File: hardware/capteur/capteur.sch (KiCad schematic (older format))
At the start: 38 parts, among them J1 Pluvio, J10 RJ45, J11 Term_sel, J12 Conn_01x05_Male, J2 Conn_01x02_Male, J3 NMEA0183 (wind), J4 Conn_01x02_Male, J5 Conn_01x02_Male, J6 Conn_01x02_Male, J7 Conn_01x03_Male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

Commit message: L'empreinte utilisée pour le connecteur RJ45 MP002453 est inversée; modification du nom utilisé pour le montrer.
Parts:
- J10: footprint local:multicomp_MP002453 -> local:multicomp_MP002453-swappedpins
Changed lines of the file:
@@
 F 0 "J10" H 9270 4046 50  0000 R CNN
 F 1 "RJ45" H 9270 3955 50  0000 R CNN
-F 2 "local:multicomp_MP002453" V 9600 3975 50  0001 C CNN
+F 2 "local:multicomp_MP002453-swappedpins" V 9600 3975 50  0001 C CNN
 F 3 "~" V 9600 3975 50  0001 C CNN
 	1    9600 3950

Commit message: Nome les signaux SCL et SDA (pour repérage facile)
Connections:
- net SCL: now reaches J9.2 (Pin_2), R6.2, U1.14 (SCL/SCK/RC3)
- net SDA: now reaches J9.1 (Pin_1), R5.2, U1.15 (SDA/SDI/RC4)
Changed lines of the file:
@@
 	5400 5150 5400 5250
 Connection ~ 5400 5150
+Text Label 5450 4950 0    50   ~ 0
+SCL
+Text Label 5450 5050 0    50   ~ 0
+SDA
 $EndSCHEMATC

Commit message: capteur: Update schematic for v2 switch to pic18f27q84, change CAN transeiver reference (it's pin-compatible), switch regulators to LDL1117S50/mic5504-3.3. Also use a RJ45 connector with the right pinout.
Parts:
- removed C5: 10uF, Capacitor_SMD:C_1210_3225Metric_Pad1.33x2.70mm_HandSolder, symbol Device:C_Small
- C10, C9: value 10uF -> 1uF; footprint Capacitor_SMD:C_1210_3225Metric_Pad1.33x2.70mm_HandSolder -> Capacitor_SMD:C_0805_2012Metric_Pad1.18x1.45mm_HandSolder
- J10: footprint local:multicomp_MP002453-swappedpins -> local:multicomp_MP002453
- U1: value PIC18F26K80_ISS -> PIC18F27Q84_ISS; symbol MCU_Microchip_PIC18:PIC18F26K80_ISS -> microchip-local:PIC18F27Q84; P/N (none) -> PIC18F27Q84_ISS
- U2: value MCP2542FDxMF -> TLE9250VSJXUMA1; P/N (none) -> TLE9250VSJXUMA1
- U3: value uA7833 -> mic5504-3.3; footprint Package_TO_SOT_SMD:SOT-223-3_TabPin2 -> Package_TO_SOT_SMD:SOT-23-5_HandSoldering; symbol Regulator_Linear:uA7805 -> Regulator_Linear:MIC5504-3.3YM5; P/N (none) -> mic5504-3.3
- U4: value uA7805 -> LDL1117S50; symbol Regulator_Linear:uA7805 -> Regulator_Linear:LD1117S50TR_SOT223; P/N (none) -> LDL1117S50
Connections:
- net +12V: now also U4.3 (VI); no longer U3.1 (IN), U4.1 (IN)
- net +3V3: now also U3.5 (VOUT); no longer U3.3 (OUT)
- net +5V: now also U3.1 (VIN), U3.3 (EN), U4.2 (VO); no longer U4.3 (OUT)
- net GND: now also U4.1 (GND); no longer U4.2 (GND)
- net at C2.1, Y1.1: now also U1.9 (OSC1/CLKIN); no longer U1.10 (OSC2/CLKOUT)
- net at C3.1, Y1.2: now also U1.10 (OSC2/CLKOUT); no longer U1.9 (OSC1/CLKIN)
- no-connect marks 2 -> 3
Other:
- moved on the sheet: J2, R2
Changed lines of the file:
@@
 $EndDescr
-$Comp
-L MCU_Microchip_PIC18:PIC18F26K80_ISS U1
-U 1 1 604422A9
-P 4600 4550
-F 0 "U1" H 4600 5617 50  0000 C CNN
-F 1 "PIC18F26K80_ISS" H 4600 5526 50  0000 C CNN
-F 2 "Package_SO:SOIC-28W_7.5x17.9mm_P1.27mm" H 4600 4300 50  0001 C CNN
-F 3 "http://ww1.microchip.com/downloads/en/DeviceDoc/39977f.pdf" H 4600 4500 50  0001 C CNN
-	1    4600 4550
-	1    0    0    -1
-$EndComp
 $Comp
 L Interface_CAN_LIN:MCP2542FDxMF U2
@@
 P 6700 4150
 F 0 "U2" H 6850 3900 50  0000 C CNN
-F 1 "MCP2542FDxMF" H 7050 3750 50  0000 C CNN
+F 1 "TLE9250VSJXUMA1" H 7050 3750 50  0000 C CNN
 F 2 "Package_SO:SOIC-8_3.9x4.9mm_P1.27mm" H 6700 3650 50  0001 C CIN
-F 3 "http://ww1.microchip.com/downloads/en/DeviceDoc/MCP2542FD-4FD-MCP2542WFD-4WFD-Data-Sheet20005514B.pdf" H 6700 4150 50  0001 C CNN
+F 3 "" H 6700 4150 50  0001 C CNN
+F 4 "TLE9250VSJXUMA1" H 6700 4150 50  0001 C CNN "P/N"
 	1    6700 4150
 	1    0    0    -1
 $EndComp
 $Comp
-L Regulator_Linear:uA7805 U4
+L Regulator_Linear:LD1117S50TR_SOT223 U4
 U 1 1 604437C3
 P 8100 4000
 F 0 "U4" H 8100 4050 50  0000 C CNN
-F 1 "uA7805" H 8100 3600 50  0000 C CNN
+F 1 "LDL1117S50" H 8100 3750 50  0000 C CNN
 F 2 "Package_TO_SOT_SMD:SOT-223-3_TabPin2" H 8125 3850 50  0001 L CIN
-F 3 "http://www.ti.com/lit/ds/symlink/ua78.pdf" H 8100 3950 50  0001 C CNN
+F 3 "" H 8100 3950 50  0001 C CNN
+F 4 "LDL1117S50" H 8100 4000 50  0001 C CNN "P/N"
 	1    8100 4000
 	-1   0    0    1
@@
 	3150 4600 3150 4500
 $Comp
-L Device:C_Small C5
-U 1 1 60447786
-P 3550 5050
-F 0 "C5" H 3458 5004 50  0000 R CNN
-F 1 "10uF" H 3458 5095 50  0000 R CNN
-F 2 "Capacitor_SMD:C_1210_3225Metric_Pad1.33x2.70mm_HandSolder" H 3550 5050 50  0001 C CNN
-F 3 "~" H 3550 5050 50  0001 C CNN
-	1    3550 5050
-	-1   0    0    1
-$EndComp
-$Comp
 L Device:C_Small C4
 U 1 1 6044A0E3
@@
 Connection ~ 3700 4850
 Wire Wire Line
-	3800 4950 3550 4950
-Wire Wire Line
 	3850 5150 3800 5150
 Connection ~ 3800 5150
-Wire Wire Line
-	3800 5150 3550 5150
-Wire Wire Line
-	3550 5150 3400 5150
-Connection ~ 3550 5150
 Wire Wire Line
 	3400 5150 3150 5150
@@
 F 0 "J10" H 9270 4046 50  0000 R CNN
 F 1 "RJ45" H 9270 3955 50  0000 R CNN
-F 2 "local:multicomp_MP002453-swappedpins" V 9600 3975 50  0001 C CNN
+F 2 "local:multicomp_MP002453" V 9600 3975 50  0001 C CNN
 F 3 "~" V 9600 3975 50  0001 C CNN
 	1    9600 3950
@@
 P 7700 3850
 F 0 "C10" H 7850 3800 50  0000 R CNN
-F 1 "10uF" H 7950 3900 50  0000 R CNN
-F 2 "Capacitor_SMD:C_1210_3225Metric_Pad1.33x2.70mm_HandSolder" H 7700 3850 50  0001 C CNN
+F 1 "1uF" H 7950 3900 50  0000 R CNN
+F 2 "Capacitor_SMD:C_0805_2012Metric_Pad1.18x1.45mm_HandSolder" H 7700 3850 50  0001 C CNN
 F 3 "~" H 7700 3850 50  0001 C CNN
 	1    7700 3850
@@
 Connection ~ 8450 4000
 Connection ~ 8950 4050
-$Comp
-L Device:R_Small R2
-U 1 1 6048396A
-P 3500 4350
-F 0 "R2" V 3400 4350 50  0000 C CNN
-F 1 "10K" V 3500 4350 50  0000 C CNN
-F 2 "Resistor_THT:R_Axial_DIN0207_L6.3mm_D2.5mm_P7.62mm_Horizontal" H 3500 4350 50  0001 C CNN
-F 3 "~" H 3500 4350 50  0001 C CNN
-	1    3500 4350
-	0    1    1    0
-$EndComp
-$Comp
-L power:+3.3V #PWR03
-U 1 1 60484075
-P 3350 4300
-F 0 "#PWR03" H 3350 4150 50  0001 C CNN
-F 1 "+3.3V" H 3365 4473 50  0000 C CNN
-F 2 "" H 3350 4300 50  0001 C CNN
-F 3 "" H 3350 4300 50  0001 C CNN
-	1    3350 4300
-	1    0    0    -1
-$EndComp
-Wire Wire Line
-	3800 4350 3600 4350
-Wire Wire Line
-	3400 4350 3350 4350
-Wire Wire Line
-	3350 4350 3350 4300
-Text Label 3600 4350 0    50   ~ 0
-MCLR
 $Comp
 L Connector:Conn_01x05_Male J12
@@
 Wire Wire Line
 	8900 4000 8900 4050
-Wire Wire Line
-	8450 4000 8550 4000
-$Comp
-L Regulator_Linear:uA7805 U3
+$Comp
+L Regulator_Linear:MIC5504-3.3YM5 U3
 U 1 1 604B439A
 P 8100 3400
 F 0 "U3" H 8100 3450 50  0000 C CNN
-F 1 "uA7833" H 8100 3000 50  0000 C CNN
-F 2 "Package_TO_SOT_SMD:SOT-223-3_TabPin2" H 8125 3250 50  0001 L CIN
-F 3 "http://www.ti.com/lit/ds/symlink/ua78.pdf" H 8100 3350 50  0001 C CNN
+F 1 "mic5504-3.3" H 8100 3000 50  0000 C CNN
+F 2 "Package_TO_SOT_SMD:SOT-23-5_HandSoldering" H 8125 3250 50  0001 L CIN
+F 3 "" H 8100 3350 50  0001 C CNN
+F 4 "mic5504-3.3" H 8100 3400 50  0001 C CNN "P/N"
 	1    8100 3400
 	-1   0    0    1
@@
 P 7700 3250
 F 0 "C9" H 7850 3200 50  0000 R CNN
-F 1 "10uF" H 7950 3300 50  0000 R CNN
-F 2 "Capacitor_SMD:C_1210_3225Metric_Pad1.33x2.70mm_HandSolder" H 7700 3250 50  0001 C CNN
+F 1 "1uF" H 7950 3300 50  0000 R CNN
+F 2 "Capacitor_SMD:C_0805_2012Metric_Pad1.18x1.45mm_HandSolder" H 7700 3250 50  0001 C CNN
 F 3 "~" H 7700 3250 50  0001 C CNN
 	1    7700 3250
@@
 Wire Wire Line
 	7700 3400 7700 3350
-Connection ~ 7700 3400
-Wire Wire Line
-	7700 3400 7800 3400
 Wire Wire Line
 	7700 3150 7700 3100
@@
 Wire Wire Line
 	8650 3750 8450 3750
-Wire Wire Line
-	8550 3400 8550 4000
-Wire Wire Line
-	8400 3400 8550 3400
-Connection ~ 8550 4000
-Wire Wire Line
-	8550 4000 8900 4000
 $Comp
 L power:GND #PWR09
@@
 L Connector:Conn_01x02_Male J2
 U 1 1 605531D0
-P 3400 3750
-F 0 "J2" H 3508 3931 50  0000 C CNN
-F 1 "Conn_01x02_Male" H 3508 3840 50  0000 C CNN
-F 2 "te:282834-2_1" H 3400 3750 50  0001 C CNN
-F 3 "~" H 3400 3750 50  0001 C CNN
-	1    3400 3750
+P 3400 3850
+F 0 "J2" H 3350 3800 50  0000 C CNN
+F 1 "Conn_01x02_Male" H 3500 3700 50  0000 C CNN
+F 2 "te:282834-2_1" H 3400 3850 50  0001 C CNN
+F 3 "~" H 3400 3850 50  0001 C CNN
+	1    3400 3850
 	1    0    0    -1
 $EndComp
@@
 Connection ~ 3150 4500
 Wire Wire Line
-	3650 4000 3650 4150
-Wire Wire Line
-	3650 4150 3800 4150
-Wire Wire Line
-	3600 3750 3800 3750
-Wire Wire Line
-	3800 3850 3600 3850
+	3600 3850 3800 3850
+Wire Wire Line
+	3800 3950 3600 3950
 $Comp
 L Device:R_Small R1
@@
 	3050 4500 2850 4500
 Connection ~ 3050 4500
-Wire Wire Line
-	3650 4000 3050 4000
 Connection ~ 3050 4000
 Wire Wire Line
@@
 Wire Wire Line
 	3050 4000 2850 4000
-NoConn ~ 3800 3950
+NoConn ~ 3800 4250
 NoConn ~ 3800 4050
 $Comp
@@
 	1    0    0    -1
 $EndComp
-$Comp
-L power:PWR_FLAG #FLG01
-U 1 1 606683BC
-P 8550 3350
-F 0 "#FLG01" H 8550 3425 50  0001 C CNN
-F 1 "PWR_FLAG" H 8550 3523 50  0000 C CNN
-F 2 "" H 8550 3350 50  0001 C CNN
-F 3 "~" H 8550 3350 50  0001 C CNN
-	1    8550 3350
-	1    0    0    -1
-$EndComp
 Wire Wire Line
 	8650 3050 8650 3100
 Connection ~ 8650 3100
-Wire Wire Line
-	8550 3350 8550 3400
-Connection ~ 8550 3400
 $Comp
 L Connector_Generic:Conn_02x03_Odd_Even J11
@@
 	10700 4150 10850 4150
 $Comp
-L power:GND #PWR?
+L power:GND #PWR0101
 U 1 1 6069A878
 P 5500 5150
-F 0 "#PWR?" H 5500 4900 50  0001 C CNN
+F 0 "#PWR0101" H 5500 4900 50  0001 C CNN
 F 1 "GND" H 5505 4977 50  0000 C CNN
 F 2 "" H 5500 5150 50  0001 C CNN
@@
 Text Label 5450 5050 0    50   ~ 0
 SDA
+Wire Wire Line
+	8450 4000 8900 4000
+$Comp
+L power:+5V #PWR0102
+U 1 1 62317E9C
+P 8550 3450
+F 0 "#PWR0102" H 8550 3300 50  0001 C CNN
+F 1 "+5V" V 8565 3578 50  0000 L CNN
+F 2 "" H 8550 3450 50  0001 C CNN
+F 3 "" H 8550 3450 50  0001 C CNN
+	1    8550 3450
+	1    0    0    -1
+$EndComp
+Wire Wire Line
+	8500 3300 8500 3500
+Wire Wire Line
+	8550 3450 8550 3500
+Wire Wire Line
+	8550 3500 8500 3500
+Connection ~ 8500 3500
+Wire Wire Line
+	7700 3400 7700 3500
+Connection ~ 7700 3400
+Text Label 3600 3750 0    50   ~ 0
+MCLR
+Wire Wire Line
+	3350 3750 3350 3700
+Wire Wire Line
+	3400 3750 3350 3750
+Wire Wire Line
+	3800 3750 3600 3750
+$Comp
+L power:+3.3V #PWR03
+U 1 1 60484075
+P 3350 3700
+F 0 "#PWR03" H 3350 3550 50  0001 C CNN
+F 1 "+3.3V" H 3365 3873 50  0000 C CNN
+F 2 "" H 3350 3700 50  0001 C CNN
+F 3 "" H 3350 3700 50  0001 C CNN
+	1    3350 3700
+	1    0    0    -1
+$EndComp
+$Comp
+L Device:R_Small R2
+U 1 1 6048396A
+P 3500 3750
+F 0 "R2" V 3400 3750 50  0000 C CNN
+F 1 "10K" V 3500 3750 50  0000 C CNN
+F 2 "Resistor_THT:R_Axial_DIN0207_L6.3mm_D2.5mm_P7.62mm_Horizontal" H 3500 3750 50  0001 C CNN
+F 3 "~" H 3500 3750 50  0001 C CNN
+	1    3500 3750
+	0    1    1    0
+$EndComp
+$Comp
+L microchip-local:PIC18F27Q84 U1
+U 1 1 604422A9
+P 4600 4550
+F 0 "U1" H 4600 5617 50  0000 C CNN
+F 1 "PIC18F27Q84_ISS" H 4600 5526 50  0000 C CNN
+F 2 "Package_SO:SOIC-28W_7.5x17.9mm_P1.27mm" H 4600 4300 50  0001 C CNN
+F 3 "" H 4600 4500 50  0001 C CNN
+F 4 "PIC18F27Q84_ISS" H 4600 4550 50  0001 C CNN "P/N"
+	1    4600 4550
+	1    0    0    -1
+$EndComp
+NoConn ~ 3800 4150
+Wire Wire Line
+	3400 5150 3800 5150
+Wire Wire Line
+	3050 4000 3350 4000
+Wire Wire Line
+	3350 4000 3350 4350
+Wire Wire Line
+	3350 4350 3800 4350
 $EndSCHEMATC

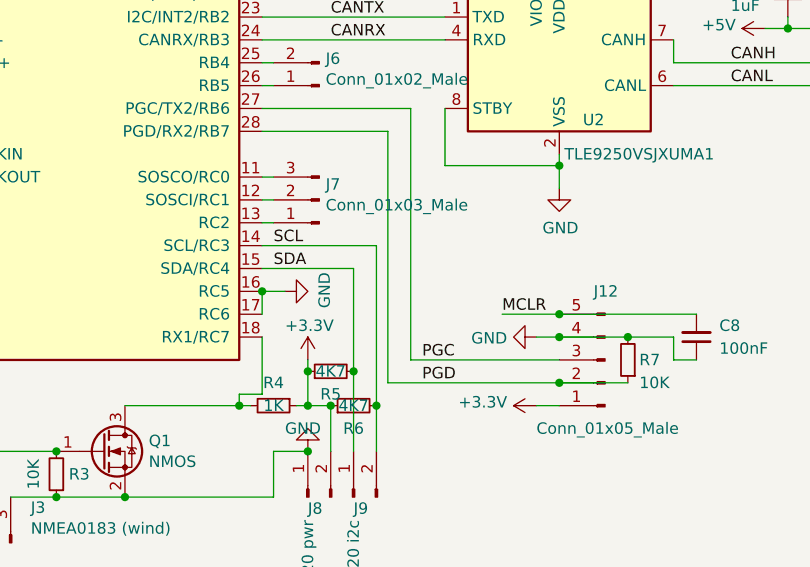
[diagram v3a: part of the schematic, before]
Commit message: capteur v2: add a LED for debug purposes.
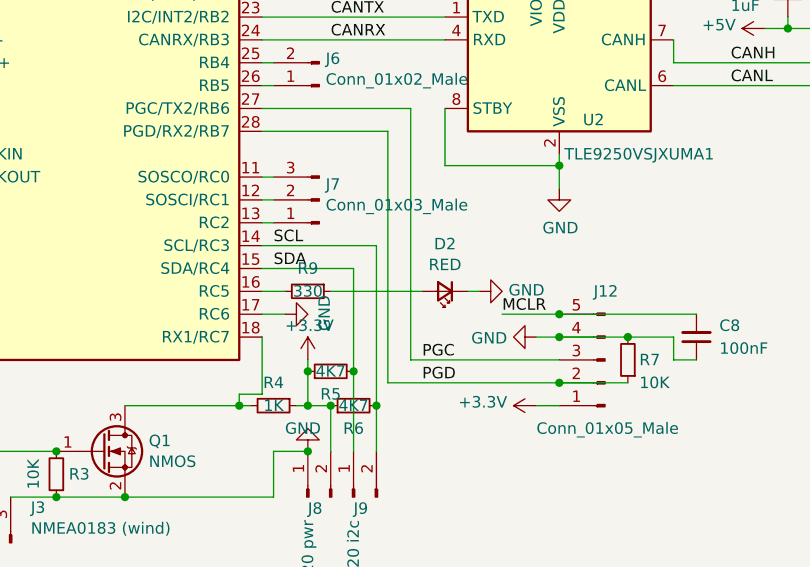
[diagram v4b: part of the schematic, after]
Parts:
- added D2: RED, LED_THT:LED_D3.0mm, symbol Device:LED_Small
- added R9: 330, Resistor_THT:R_Axial_DIN0207_L6.3mm_D2.5mm_P7.62mm_Horizontal, symbol Device:R_Small
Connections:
- net GND: now also D2.1 (K); no longer U1.16 (RC5)
- new net: R9.2, U1.16 (RC5)
- new net: D2.2 (A), R9.1
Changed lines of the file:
@@
 L power:GND #PWR0101
 U 1 1 6069A878
-P 5500 5150
-F 0 "#PWR0101" H 5500 4900 50  0001 C CNN
-F 1 "GND" H 5505 4977 50  0000 C CNN
-F 2 "" H 5500 5150 50  0001 C CNN
-F 3 "" H 5500 5150 50  0001 C CNN
-	1    5500 5150
+P 5500 5250
+F 0 "#PWR0101" H 5500 5000 50  0001 C CNN
+F 1 "GND" H 5505 5077 50  0000 C CNN
+F 2 "" H 5500 5250 50  0001 C CNN
+F 3 "" H 5500 5250 50  0001 C CNN
+	1    5500 5250
 	0    -1   -1   0
 $EndComp
-Wire Wire Line
-	5500 5150 5400 5150
-Wire Wire Line
-	5400 5150 5400 5250
-Connection ~ 5400 5150
 Text Label 5450 4950 0    50   ~ 0
 SCL
@@
 Wire Wire Line
 	3350 4350 3800 4350
+Wire Wire Line
+	5500 5250 5400 5250
+$Comp
+L Device:R_Small R9
+U 1 1 62325BC6
+P 5600 5150
+F 0 "R9" V 5500 5150 50  0000 C CNN
+F 1 "330" V 5600 5150 50  0000 C CNN
+F 2 "Resistor_THT:R_Axial_DIN0207_L6.3mm_D2.5mm_P7.62mm_Horizontal" H 5600 5150 50  0001 C CNN
+F 3 "~" H 5600 5150 50  0001 C CNN
+	1    5600 5150
+	0    1    1    0
+$EndComp
+$Comp
+L Device:LED_Small D2
+U 1 1 6232694A
+P 6200 5150
+F 0 "D2" H 6200 4943 50  0000 C CNN
+F 1 "RED" H 6200 5034 50  0000 C CNN
+F 2 "LED_THT:LED_D3.0mm" V 6200 5150 50  0001 C CNN
+F 3 "~" V 6200 5150 50  0001 C CNN
+	1    6200 5150
+	-1   0    0    1
+$EndComp
+$Comp
+L power:GND #PWR020
+U 1 1 6232756D
+P 6350 5150
+F 0 "#PWR020" H 6350 4900 50  0001 C CNN
+F 1 "GND" V 6355 5022 50  0000 R CNN
+F 2 "" H 6350 5150 50  0001 C CNN
+F 3 "" H 6350 5150 50  0001 C CNN
+	1    6350 5150
+	0    -1   -1   0
+$EndComp
+Wire Wire Line
+	6350 5150 6300 5150
+Wire Wire Line
+	6100 5150 5700 5150
+Wire Wire Line
+	5500 5150 5400 5150
 $EndSCHEMATC

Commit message: On second though, keep the swappedpin connector - we already have the cable :)
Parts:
- J10: footprint local:multicomp_MP002453 -> local:multicomp_MP002453-swappedpins
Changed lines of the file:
@@
 F 0 "J10" H 9270 4046 50  0000 R CNN
 F 1 "RJ45" H 9270 3955 50  0000 R CNN
-F 2 "local:multicomp_MP002453" V 9600 3975 50  0001 C CNN
+F 2 "local:multicomp_MP002453-swappedpins" V 9600 3975 50  0001 C CNN
 F 3 "~" V 9600 3975 50  0001 C CNN
 	1    9600 3950
